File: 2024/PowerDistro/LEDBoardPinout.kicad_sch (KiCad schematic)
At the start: 1 part, among them U1 PCA9685

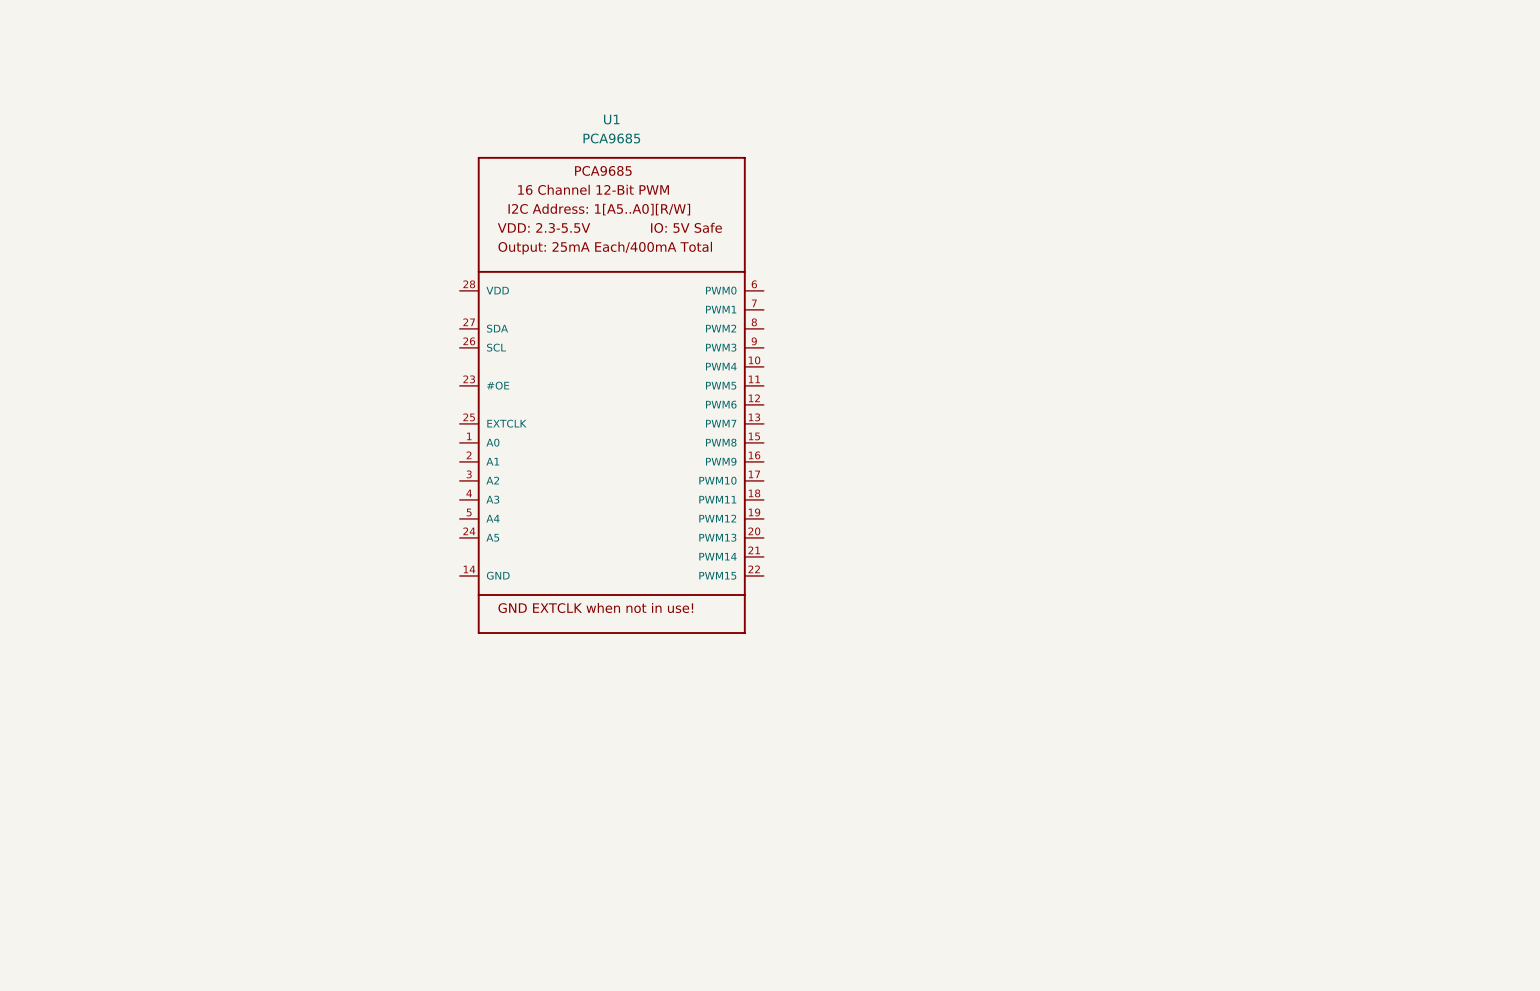
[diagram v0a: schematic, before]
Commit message: Added PCA pinout schematics
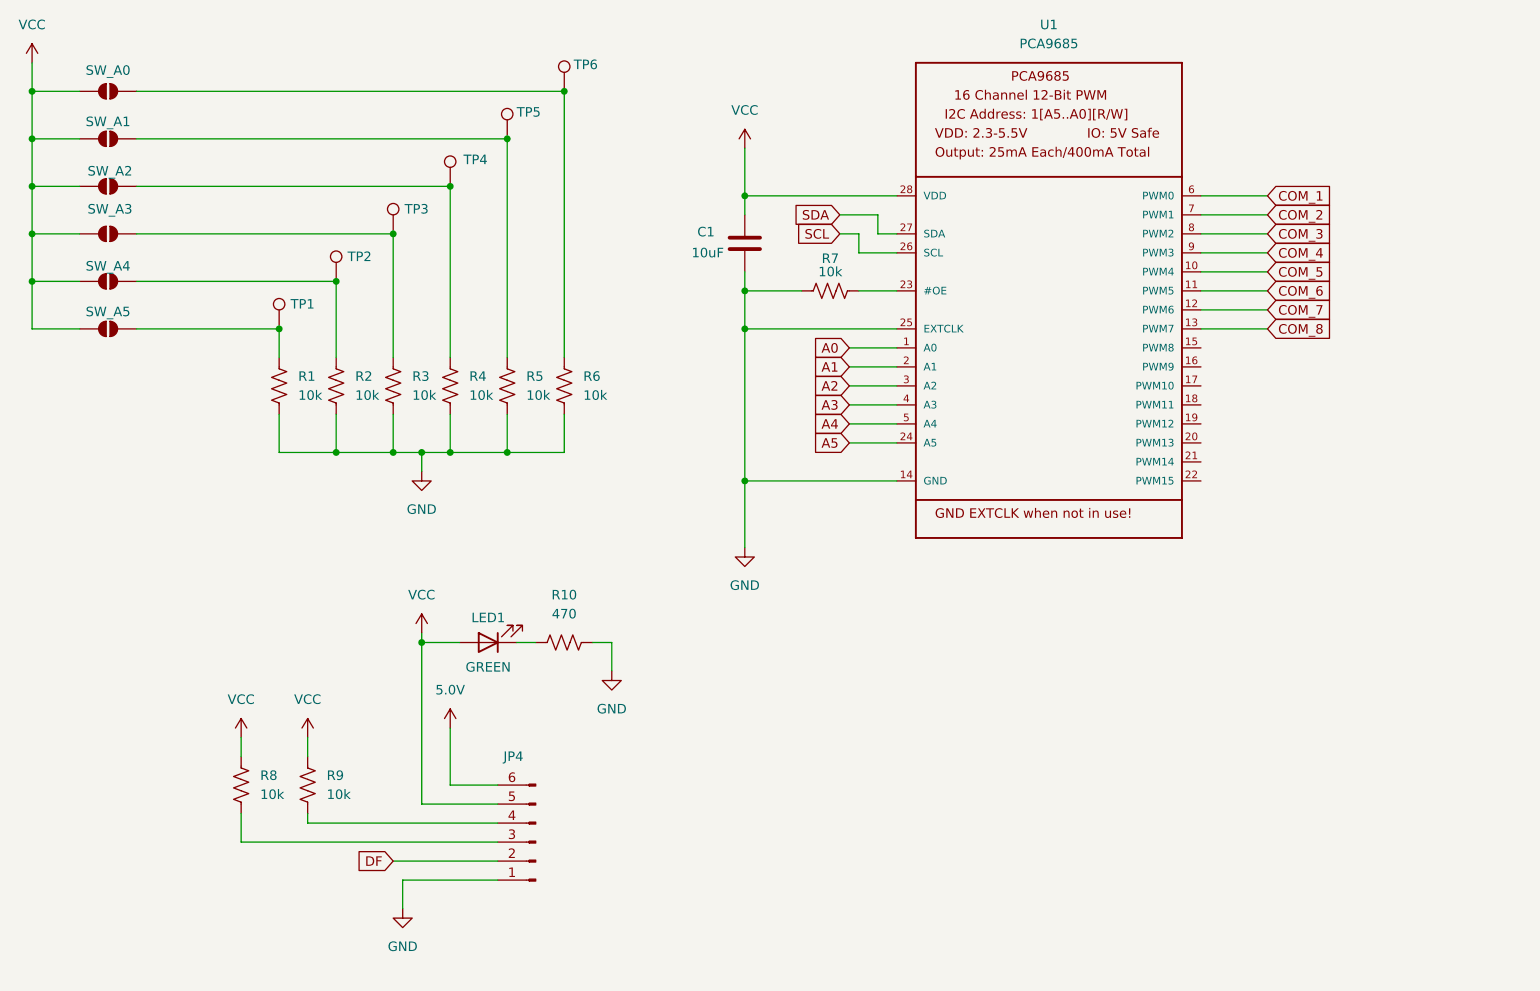
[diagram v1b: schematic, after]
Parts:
- added C1: 10uF, symbol Device:C
- added JP4: Conn_01x06_Pin, symbol Connector:Conn_01x06_Pin
- added LED1: GREEN, symbol Device:LED
- added R1, R2, R3, R4, R5, R6, R7, R8, R9: 10k, symbol Device:R_US
- added R10: 470, symbol Device:R_US
- added SW_A0, SW_A1, SW_A2, SW_A3, SW_A4, SW_A5: SolderJumper_2_Open, symbol Jumper:SolderJumper_2_Open
- added TP1, TP2, TP3, TP4, TP5, TP6: TestPoint, symbol Connector:TestPoint
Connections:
- net A0: now reaches U1.1 (A0)
- net COM_5: now reaches U1.10 (PWM4)
- net COM_6: now reaches U1.11 (PWM5)
- net COM_7: now reaches U1.12 (PWM6)
- net COM_8: now reaches U1.13 (PWM7)
- net GND: now reaches U1.14 (GND)
- net GND: now also U1.25 (EXTCLK), C1.2, JP4.1 (Pin_1), R1.2, R10.2, R2.2, R3.2, R4.2, R5.2, R6.2, R7.2
- net A1: now reaches U1.2 (A1)
- net at U1.23 (#OE): now also R7.1
- net A5: now reaches U1.24 (A5)
- net SCL: now reaches U1.26 (SCL)
- net SDA: now reaches U1.27 (SDA)
- net VCC: now reaches U1.28 (VDD)
- net VCC: now also C1.1, JP4.5 (Pin_5), LED1.2 (A), R8.1, R9.1, SW_A0.1 (A), SW_A1.1 (A), SW_A2.1 (A), SW_A3.1 (A), SW_A4.1 (A), SW_A5.1 (A)
- net A2: now reaches U1.3 (A2)
- net A3: now reaches U1.4 (A3)
- net A4: now reaches U1.5 (A4)
- net COM_1: now reaches U1.6 (PWM0)
- net COM_2: now reaches U1.7 (PWM1)
- net COM_3: now reaches U1.8 (PWM2)
- net COM_4: now reaches U1.9 (PWM3)
- new net: R1.1, SW_A5.2 (B), TP1.1
- new net: JP4.3 (Pin_3), R8.2
- new net: JP4.4 (Pin_4), R9.2
- new net: R2.1, SW_A4.2 (B), TP2.1
- new net: R6.1, SW_A0.2 (B), TP6.1
- new net: LED1.1 (K), R10.1
- new net: R3.1, SW_A3.2 (B), TP3.1
- new net: R5.1, SW_A1.2 (B), TP5.1
- new net: R4.1, SW_A2.2 (B), TP4.1
- new net 5.0V: JP4.6 (Pin_6)
- new net DF: JP4.2 (Pin_2)
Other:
- moved on the sheet: U1

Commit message: finish pca schematic
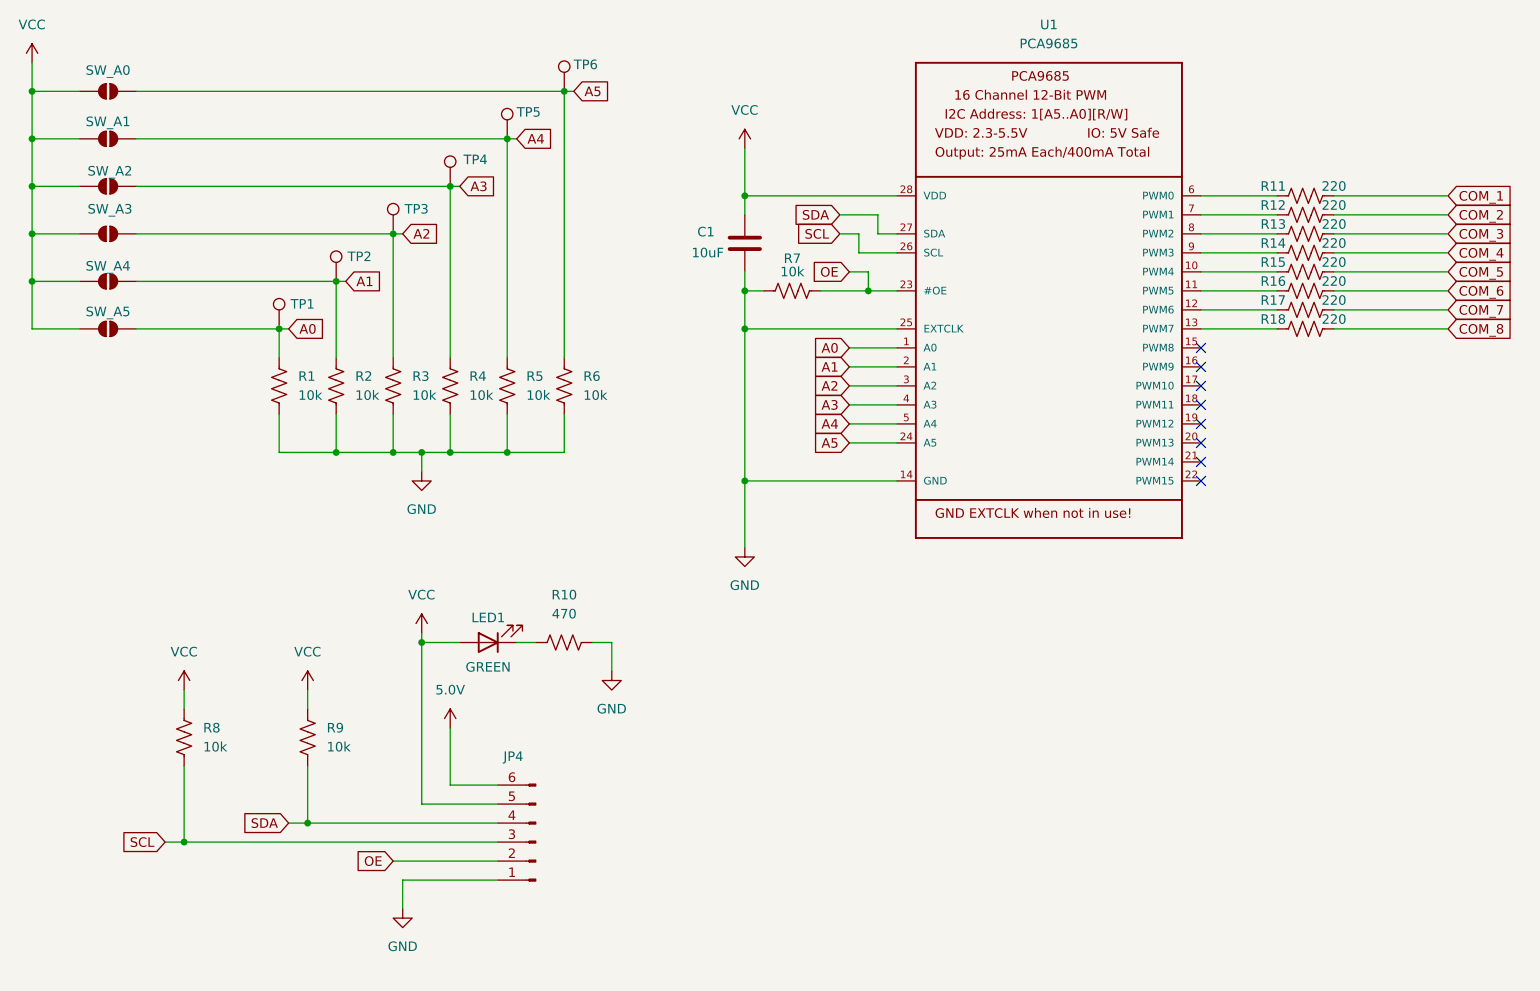
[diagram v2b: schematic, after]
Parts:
- added R11, R12, R13, R14, R15, R16, R17, R18: 220, symbol Device:R_US
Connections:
- net DF is gone; now on net OE: JP4.2 (Pin_2)
- net A0: now also R1.1, SW_A5.2 (B), TP1.1
- net A1: now also R2.1, SW_A4.2 (B), TP2.1
- net A2: now also R3.1, SW_A3.2 (B), TP3.1
- net A3: now also R4.1, SW_A2.2 (B), TP4.1
- net A4: now also R5.1, SW_A1.2 (B), TP5.1
- net A5: now also R6.1, SW_A0.2 (B), TP6.1
- net COM_1: now also R11.2; no longer U1.6 (PWM0)
- net COM_2: now also R12.2; no longer U1.7 (PWM1)
- net COM_3: now also R13.2; no longer U1.8 (PWM2)
- net COM_4: now also R14.2; no longer U1.9 (PWM3)
- net COM_5: now also R15.2; no longer U1.10 (PWM4)
- net COM_6: now also R16.2; no longer U1.11 (PWM5)
- net COM_7: now also R17.2; no longer U1.12 (PWM6)
- net COM_8: now also R18.2; no longer U1.13 (PWM7)
- net SCL: now also JP4.3 (Pin_3), R8.2
- net SDA: now also JP4.4 (Pin_4), R9.2
- net OE: now reaches R7.1, U1.23 (#OE)
- new net: R18.1, U1.13 (PWM7)
- new net: R15.1, U1.10 (PWM4)
- new net: R16.1, U1.11 (PWM5)
- new net: R17.1, U1.12 (PWM6)
- new net: R11.1, U1.6 (PWM0)
- new net: R12.1, U1.7 (PWM1)
- new net: R13.1, U1.8 (PWM2)
- new net: R14.1, U1.9 (PWM3)
- no-connect marks 0 -> 8
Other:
- moved on the sheet: R7, R8, R9

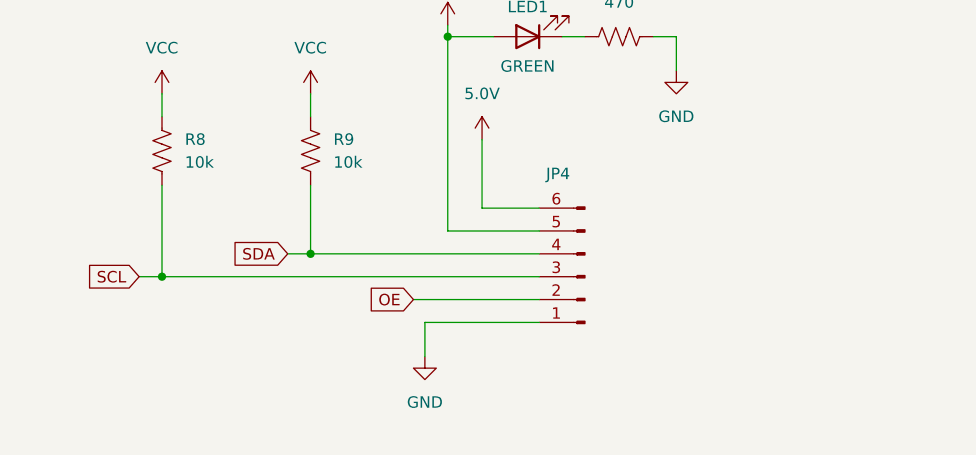
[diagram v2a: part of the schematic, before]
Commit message: added JST_SM06B-GHS-TB_LF__SN_ symbol and footprint into PCA pinout
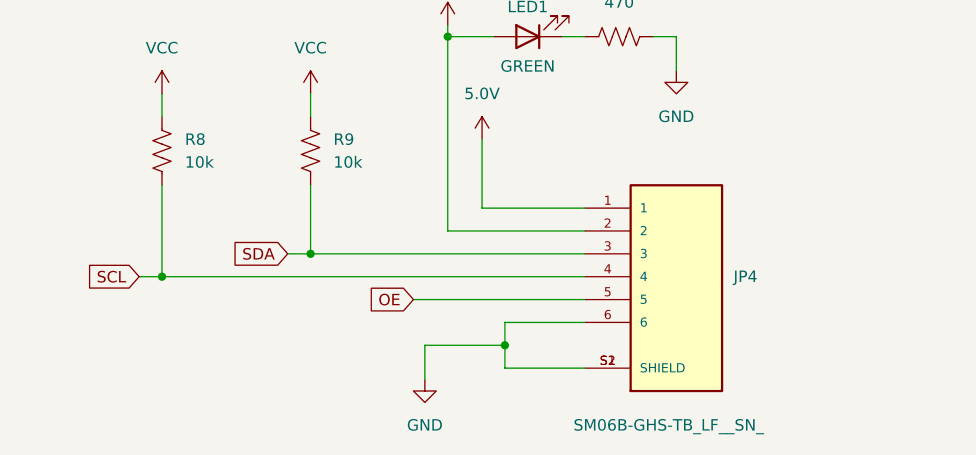
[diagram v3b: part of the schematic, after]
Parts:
- removed JP4: Conn_01x06_Pin, symbol Connector:Conn_01x06_Pin
- added JP4: SM06B-GHS-TB_LF__SN_, SM06B-GHS-TB_LF__SN_:JST_SM06B-GHS-TB_LF__SN_, symbol PowerDistro:SM06B-GHS-TB_LF__SN_
- LED1: footprint (none) -> LED_SMD:LED_0603_1608Metric
- R1, R10, R11, R12, R13, R14, R15, R16, R17, R18, R2, R3, R4, R5, R6, R7, R8, R9: footprint (none) -> Resistor_SMD:R_0603_1608Metric
- SW_A0, SW_A1, SW_A2, SW_A3, SW_A4, SW_A5: footprint (none) -> Jumper:SolderJumper-2_P1.3mm_Open_RoundedPad1.0x1.5mm
- TP1, TP2, TP3, TP4, TP5, TP6: footprint (none) -> TestPoint:TestPoint_Pad_D2.5mm
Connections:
- net 5.0V: now also JP4.1
- net GND: now also JP4.6, JP4.S1 (SHIELD), JP4.S2 (SHIELD)
- net OE: now also JP4.5
- net SCL: now also JP4.4
- net SDA: now also JP4.3
- net VCC: now also JP4.2
